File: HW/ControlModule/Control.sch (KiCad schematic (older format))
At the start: 88 parts, among them J1 Conn_01x03, J2 Conn_01x03, J3 Conn_01x03, J4 Conn_01x03, J5 Conn_01x03, J6 Conn_01x03, J7 Conn_01x03, J8 Conn_01x03, U1 AD8629, U2 STM32L476VETx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

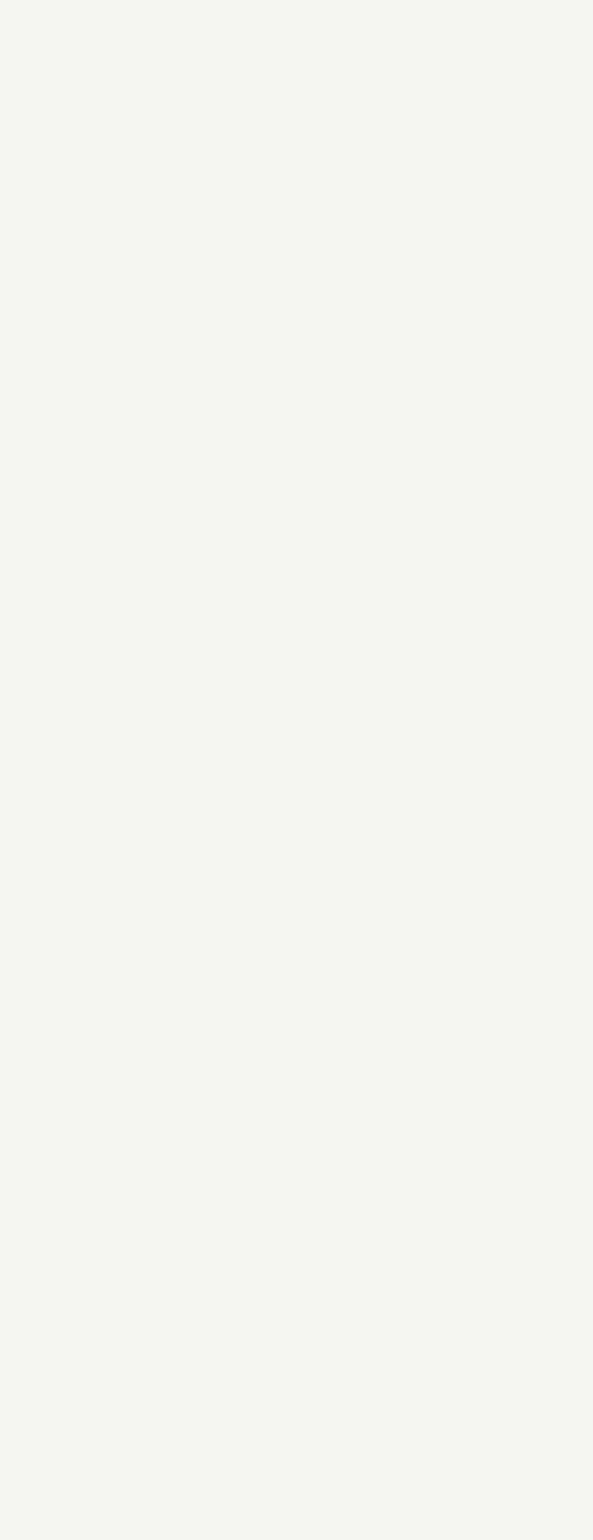
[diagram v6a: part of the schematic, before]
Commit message: migrated HW
- Changed STM32L476 to STM32L496  (STM32L476  did not support ADC->DFSDM config)
- Created new SW project "STM32L496_DigitalCurrentSinkV3"
- Confirmed compilation success with all libs and firmware.
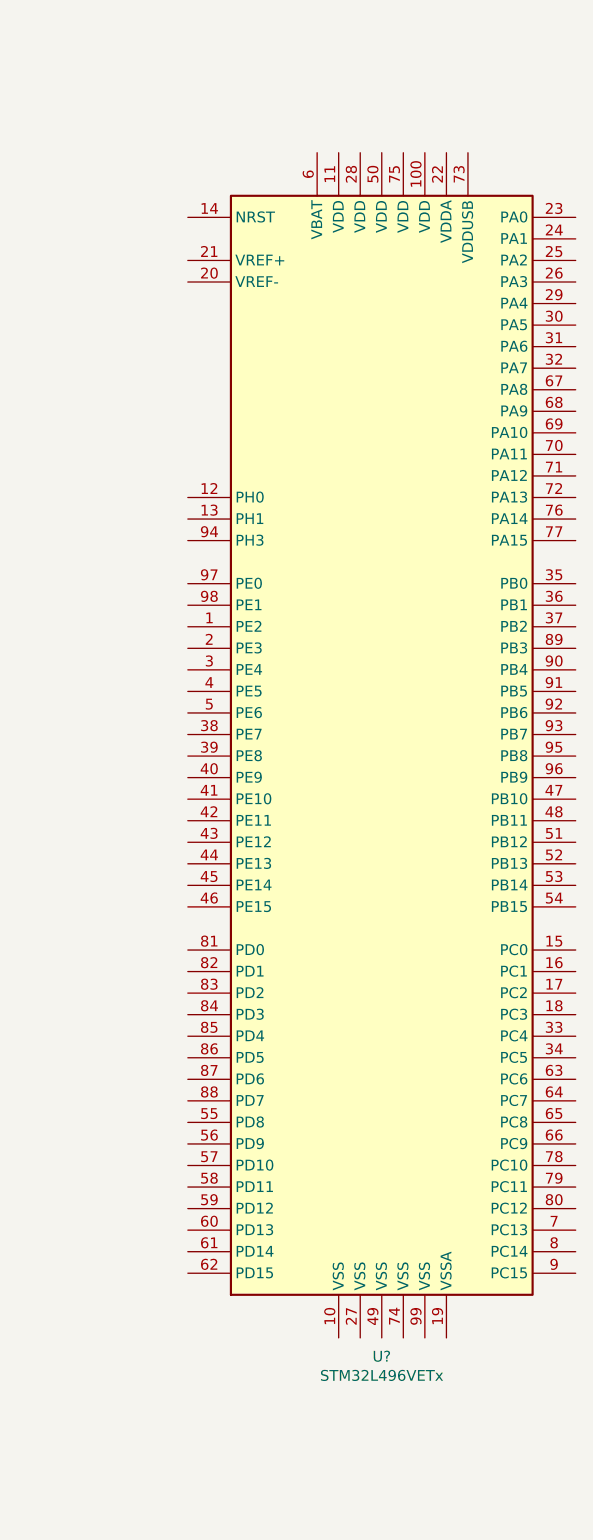
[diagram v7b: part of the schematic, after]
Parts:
- added U?: STM32L496VETx, Package_QFP:LQFP-100_14x14mm_P0.5mm, symbol MCU_ST_STM32L4:STM32L496VETx
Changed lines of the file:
@@
 Text Notes 1550 4400 0    50   ~ 0
 TO BYPASS:\n1) Remove U1\n2) Solder JP5, JP6, R1 and R2\n3) Populate R3, R4 with 100R\nand C1, C2 with 100nF for FC=15KHz
+$Comp
+L MCU_ST_STM32L4:STM32L496VETx U?
+U 1 1 5D6151A4
+P 26700 6900
+F 0 "U?" H 26700 4013 50  0000 C CNN
+F 1 "STM32L496VETx" H 26700 3924 50  0000 C CNN
+F 2 "Package_QFP:LQFP-100_14x14mm_P0.5mm" H 26000 4300 50  0001 R CNN
+F 3 "http://www.st.com/st-web-ui/static/active/en/resource/technical/document/datasheet/DM00284211.pdf" H 26700 6900 50  0001 C CNN
+	1    26700 6900
+	1    0    0    -1
+$EndComp
 $EndSCHEMATC

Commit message: Tested STM32L496VG upgrade, replaced symbol in schematic
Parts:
- removed U2: STM32L476VETx, Package_QFP:LQFP-100_14x14mm_P0.5mm, symbol MCU_ST_STM32L4:STM32L476VETx
- removed U?: STM32L496VETx, Package_QFP:LQFP-100_14x14mm_P0.5mm, symbol MCU_ST_STM32L4:STM32L496VETx
- added U2: STM32L496VGTx, Package_QFP:LQFP-100_14x14mm_P0.5mm, symbol MCU_ST_STM32L4:STM32L496VGTx
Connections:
- net +3.3VA: now also U2.21 (VREF+), U2.22 (VDDA)
- net +3V3: now also U2.100 (VDD), U2.11 (VDD), U2.28 (VDD), U2.50 (VDD), U2.73 (VDDUSB), U2.75 (VDD)
- net ADCS1: now also U2.24 (PA1)
- net ADCS2: now also U2.25 (PA2)
- net BTN1: now also U2.57 (PD10)
- net BTN2: now also U2.58 (PD11)
- net BTN3: now also U2.59 (PD12)
- net BTN4: now also U2.60 (PD13)
- net DACOUT1: now also U2.29 (PA4)
- net DACOUT2: now also U2.30 (PA5)
- net GNDS: now also U2.10 (VSS), U2.19 (VSSA), U2.20 (VREF-), U2.27 (VSS), U2.49 (VSS), U2.6 (VBAT), U2.74 (VSS), U2.99 (VSS)
- net KEYPAD1: now also U2.38 (PE7)
- net KEYPAD2: now also U2.39 (PE8)
- net KEYPAD3: now also U2.40 (PE9)
- net KEYPAD4: now also U2.41 (PE10)
- net KEYPAD5: now also U2.35 (PB0)
- net KEYPAD6: now also U2.36 (PB1)
- net KEYPAD7: now also U2.37 (PB2)
- net NRST: now also U2.14 (NRST)
- net OLED_SCL: now also U2.92 (PB6)
- net OLED_SDA: now also U2.93 (PB7)
- net SWCLK: now also U2.76 (PA14)
- net SWDIO: now also U2.72 (PA13)
- net SWO: now also U2.89 (PB3)
- net at R5.1: now also U2.94 (PH3)
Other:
- moved on the sheet: C16, C23, R5
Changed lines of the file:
@@
 	4100 6450 4100 7700
 Connection ~ 4100 7700
-$Comp
-L MCU_ST_STM32L4:STM32L476VETx U2
-U 1 1 5E90D5BD
-P 12800 6900
-F 0 "U2" H 11350 8400 50  0000 C CNN
-F 1 "STM32L476VETx" H 11425 8225 50  0000 C CNN
-F 2 "Package_QFP:LQFP-100_14x14mm_P0.5mm" H 12100 4300 50  0001 R CNN
-F 3 "http://www.st.com/st-web-ui/static/active/en/resource/technical/document/datasheet/DM00108832.pdf" H 12800 6900 50  0001 C CNN
-F 4 "511-STM32L476VET6" H 12800 6900 50  0001 C CNN "MouserNo"
-F 5 "STM32L476VET6" H 12800 6900 50  0001 C CNN "Mfr. No:"
-F 6 "STMicroelectronics" H 12800 6900 50  0001 C CNN "Mfr:"
-F 7 "497-15878-ND" H 12800 6900 50  0001 C CNN "DigikeyNo"
-F 8 "896-7695" H 12800 6900 50  0001 C CNN "RSComponentsNo"
-	1    12800 6900
-	1    0    0    -1
-$EndComp
 Wire Wire Line
 	12600 4200 12600 2050
@@
 L Device:R R5
 U 1 1 5E92B717
-P 10000 4850
-F 0 "R5" H 10070 4896 50  0000 L CNN
-F 1 "10K" H 10070 4805 50  0000 L CNN
-F 2 "Resistor_SMD:R_0402_1005Metric" V 9930 4850 50  0001 C CNN
-F 3 "~" H 10000 4850 50  0001 C CNN
-	1    10000 4850
-	1    0    0    -1
-$EndComp
-Wire Wire Line
-	10000 5000 10000 5200
+P 11550 6250
+F 0 "R5" H 11620 6296 50  0000 L CNN
+F 1 "10K" H 11620 6205 50  0000 L CNN
+F 2 "Resistor_SMD:R_0402_1005Metric" V 11480 6250 50  0001 C CNN
+F 3 "~" H 11550 6250 50  0001 C CNN
+	1    11550 6250
+	1    0    0    -1
+$EndComp
+Wire Wire Line
+	11550 6400 11550 6500
 Wire Wire Line
 	13700 4600 14800 4600
@@
 L power:GNDS #PWR014
 U 1 1 5EC17F66
-P 10000 5200
-F 0 "#PWR014" H 10000 4950 50  0001 C CNN
-F 1 "GNDS" H 10005 5027 50  0000 C CNN
-F 2 "" H 10000 5200 50  0001 C CNN
-F 3 "" H 10000 5200 50  0001 C CNN
-	1    10000 5200
+P 11550 6500
+F 0 "#PWR014" H 11550 6250 50  0001 C CNN
+F 1 "GNDS" H 11555 6327 50  0000 C CNN
+F 2 "" H 11550 6500 50  0001 C CNN
+F 3 "" H 11550 6500 50  0001 C CNN
+	1    11550 6500
 	1    0    0    -1
 $EndComp
@@
 NoConn ~ 13700 4800
 NoConn ~ 11900 5900
-NoConn ~ 11900 6000
 NoConn ~ 11900 6200
 NoConn ~ 11900 6300
@@
 NoConn ~ 11900 9400
 Wire Wire Line
-	11650 4325 11650 4575
+	11650 4125 11650 4375
 Wire Wire Line
 	6050 7850 6050 7700
@@
 Connection ~ 13100 1825
 Wire Wire Line
-	11650 4900 11900 4900
+	11650 4700 11900 4700
 $Comp
 L Device:R R8
@@
 	9500 3500 9500 4500
 Wire Wire Line
-	11825 3750 10000 3750
-Wire Wire Line
-	10000 3750 10000 4700
-Wire Wire Line
-	11825 4700 11900 4700
-Wire Wire Line
-	11825 3750 11825 4700
-Text Label 10375 5000 0    50   ~ 0
+	11900 6000 11550 6000
+Wire Wire Line
+	11550 6000 11550 6100
+Text Label 10375 4800 0    50   ~ 0
 VSSA
-Text Label 11650 4325 3    50   ~ 0
+Text Label 11650 4125 3    50   ~ 0
 VDDA
 Wire Wire Line
-	10375 5000 10750 5000
+	10375 4800 10750 4800
 $Comp
 L Device:C C16
 U 1 1 5DCD5FBA
-P 10750 4775
-F 0 "C16" H 10865 4821 50  0000 L CNN
-F 1 "100n" H 10865 4730 50  0000 L CNN
-F 2 "Capacitor_SMD:C_0402_1005Metric" H 10788 4625 50  0001 C CNN
-F 3 "~" H 10750 4775 50  0001 C CNN
-	1    10750 4775
-	1    0    0    -1
-$EndComp
-Wire Wire Line
-	10750 4625 10750 4575
-Wire Wire Line
-	10750 4575 11250 4575
-Connection ~ 11650 4575
-Wire Wire Line
-	11650 4575 11650 4900
-Wire Wire Line
-	10750 4925 10750 5000
-Connection ~ 10750 5000
-Wire Wire Line
-	10750 5000 11250 5000
+P 10750 4575
+F 0 "C16" H 10865 4621 50  0000 L CNN
+F 1 "100n" H 10865 4530 50  0000 L CNN
+F 2 "Capacitor_SMD:C_0402_1005Metric" H 10788 4425 50  0001 C CNN
+F 3 "~" H 10750 4575 50  0001 C CNN
+	1    10750 4575
+	1    0    0    -1
+$EndComp
+Wire Wire Line
+	10750 4425 10750 4375
+Wire Wire Line
+	10750 4375 11250 4375
+Connection ~ 11650 4375
+Wire Wire Line
+	11650 4375 11650 4700
+Wire Wire Line
+	10750 4725 10750 4800
+Connection ~ 10750 4800
+Wire Wire Line
+	10750 4800 11250 4800
 $Comp
 L Device:C C23
 U 1 1 5DD3B1FE
-P 11250 4775
-F 0 "C23" H 11365 4821 50  0000 L CNN
-F 1 "1u" H 11365 4730 50  0000 L CNN
-F 2 "Capacitor_SMD:C_0402_1005Metric" H 11288 4625 50  0001 C CNN
-F 3 "~" H 11250 4775 50  0001 C CNN
-	1    11250 4775
-	1    0    0    -1
-$EndComp
-Wire Wire Line
-	11250 4575 11250 4625
-Connection ~ 11250 4575
-Wire Wire Line
-	11250 4575 11650 4575
-Wire Wire Line
-	11250 4925 11250 5000
-Connection ~ 11250 5000
-Wire Wire Line
-	11250 5000 11900 5000
+P 11250 4575
+F 0 "C23" H 11365 4621 50  0000 L CNN
+F 1 "1u" H 11365 4530 50  0000 L CNN
+F 2 "Capacitor_SMD:C_0402_1005Metric" H 11288 4425 50  0001 C CNN
+F 3 "~" H 11250 4575 50  0001 C CNN
+	1    11250 4575
+	1    0    0    -1
+$EndComp
+Wire Wire Line
+	11250 4375 11250 4425
+Connection ~ 11250 4375
+Wire Wire Line
+	11250 4375 11650 4375
+Wire Wire Line
+	11250 4725 11250 4800
+Connection ~ 11250 4800
+Wire Wire Line
+	11250 4800 11900 4800
 Wire Wire Line
 	13100 9750 13500 9750
@@
 TO BYPASS:\n1) Remove U1\n2) Solder JP5, JP6, R1 and R2\n3) Populate R3, R4 with 100R\nand C1, C2 with 100nF for FC=15KHz
 $Comp
-L MCU_ST_STM32L4:STM32L496VETx U?
-U 1 1 5D6151A4
-P 26700 6900
-F 0 "U?" H 26700 4013 50  0000 C CNN
-F 1 "STM32L496VETx" H 26700 3924 50  0000 C CNN
-F 2 "Package_QFP:LQFP-100_14x14mm_P0.5mm" H 26000 4300 50  0001 R CNN
-F 3 "http://www.st.com/st-web-ui/static/active/en/resource/technical/document/datasheet/DM00284211.pdf" H 26700 6900 50  0001 C CNN
-	1    26700 6900
-	1    0    0    -1
-$EndComp
+L MCU_ST_STM32L4:STM32L496VGTx U2
+U 1 1 5D60B1FE
+P 12800 6900
+F 0 "U2" H 10975 6025 50  0000 C CNN
+F 1 "STM32L496VGTx" H 11075 5825 50  0000 C CNN
+F 2 "Package_QFP:LQFP-100_14x14mm_P0.5mm" H 12100 4300 50  0001 R CNN
+F 3 "http://www.st.com/st-web-ui/static/active/en/resource/technical/document/datasheet/DM00284211.pdf" H 12800 6900 50  0001 C CNN
+	1    12800 6900
+	1    0    0    -1
+$EndComp
+NoConn ~ 11900 5800
 $EndSCHEMATC
